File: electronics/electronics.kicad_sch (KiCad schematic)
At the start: 41 parts, among them J1 USB_C_Receptacle_USB2.0_14P, J2 AMT_102, J3 SPARK_MAX, J4 BLDC_FAN_ESC, SW1 RST, SW2 RST, SW3 SW_Push, SW4 SW_Push, SW5 SW_Push, SW6 SW_Push, U1 ESP32-S3-WROOM-1, U2 LSF0204, U3 AMS1117-3.3, U4 TPS62140, U5 AMS1117-3.3

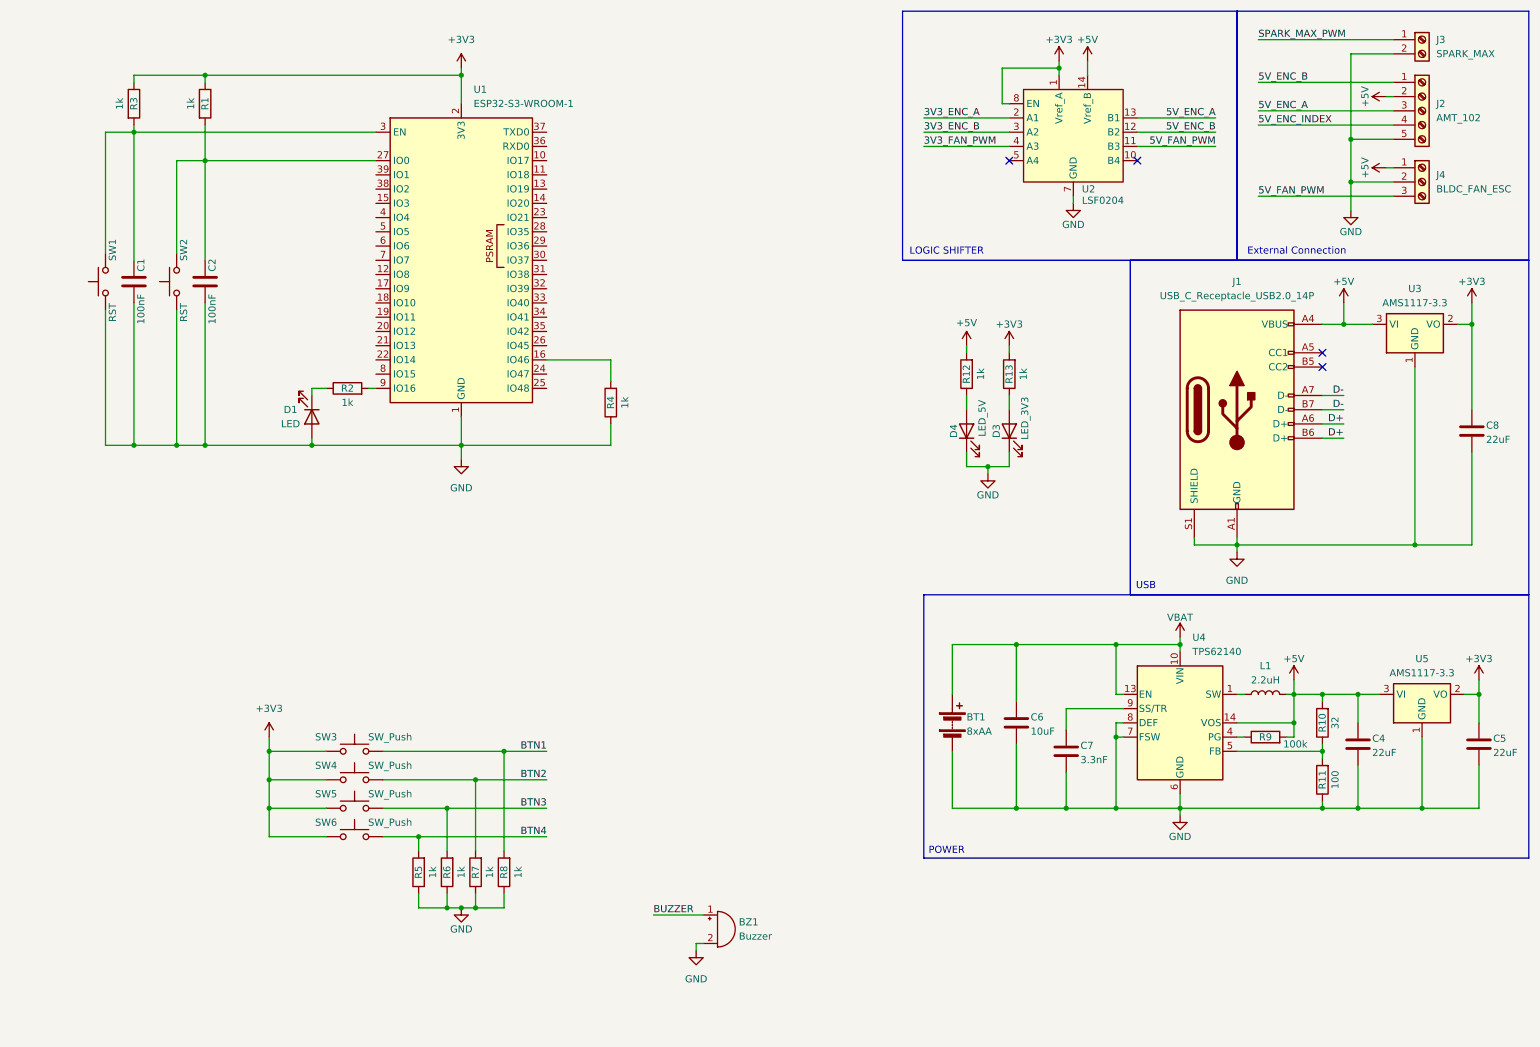
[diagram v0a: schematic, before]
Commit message: needs routing to decide pin placements
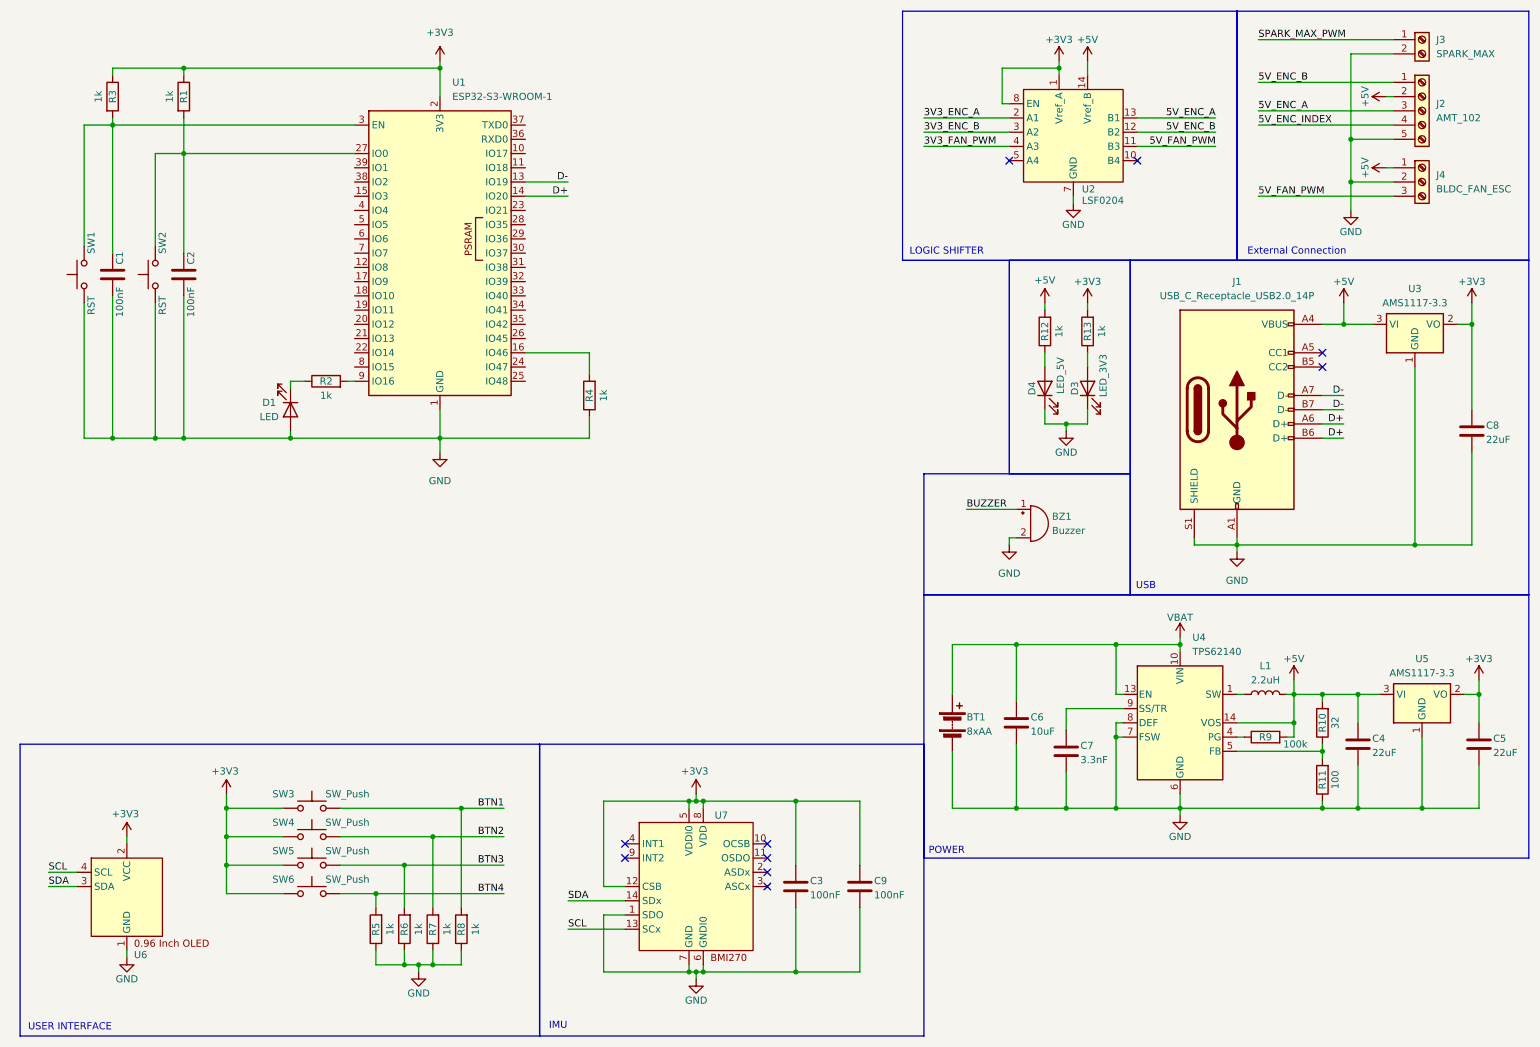
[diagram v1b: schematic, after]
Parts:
- added C3, C9: 100nF, symbol Device:C
- added U6: ~, Connector_PinHeader_2.54mm:PinHeader_1x04_P2.54mm_Vertical, symbol 0.96InchOLED:0.96_Inch_OLED
- added U7: ~, Package_LGA:Bosch_LGA-14_3x2.5mm_P0.5mm, symbol BMI270:BMI270
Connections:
- net +3V3: now also C3.1, C9.1, U6.2 (VCC), U7.12 (CSB), U7.5 (VDDI0), U7.8 (VDD)
- net D+: now also U1.14 (IO20)
- net D-: now also U1.13 (IO19)
- net GND: now also C3.2, C9.2, U6.1 (GND), U7.1 (SDO), U7.6 (GNDI0), U7.7 (GND)
- new net SCL: U6.4 (SCL), U7.13 (SCx)
- new net SDA: U6.3 (SDA), U7.14 (SDx)
- no-connect marks 4 -> 10
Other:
- note added: "IMU"
- note added: "USER INTERFACE"
- moved on the sheet: BZ1, C1, C2, D1, D3, D4, R1, R12, R13, R2, R3, R4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

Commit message: need to route switching psu correctly
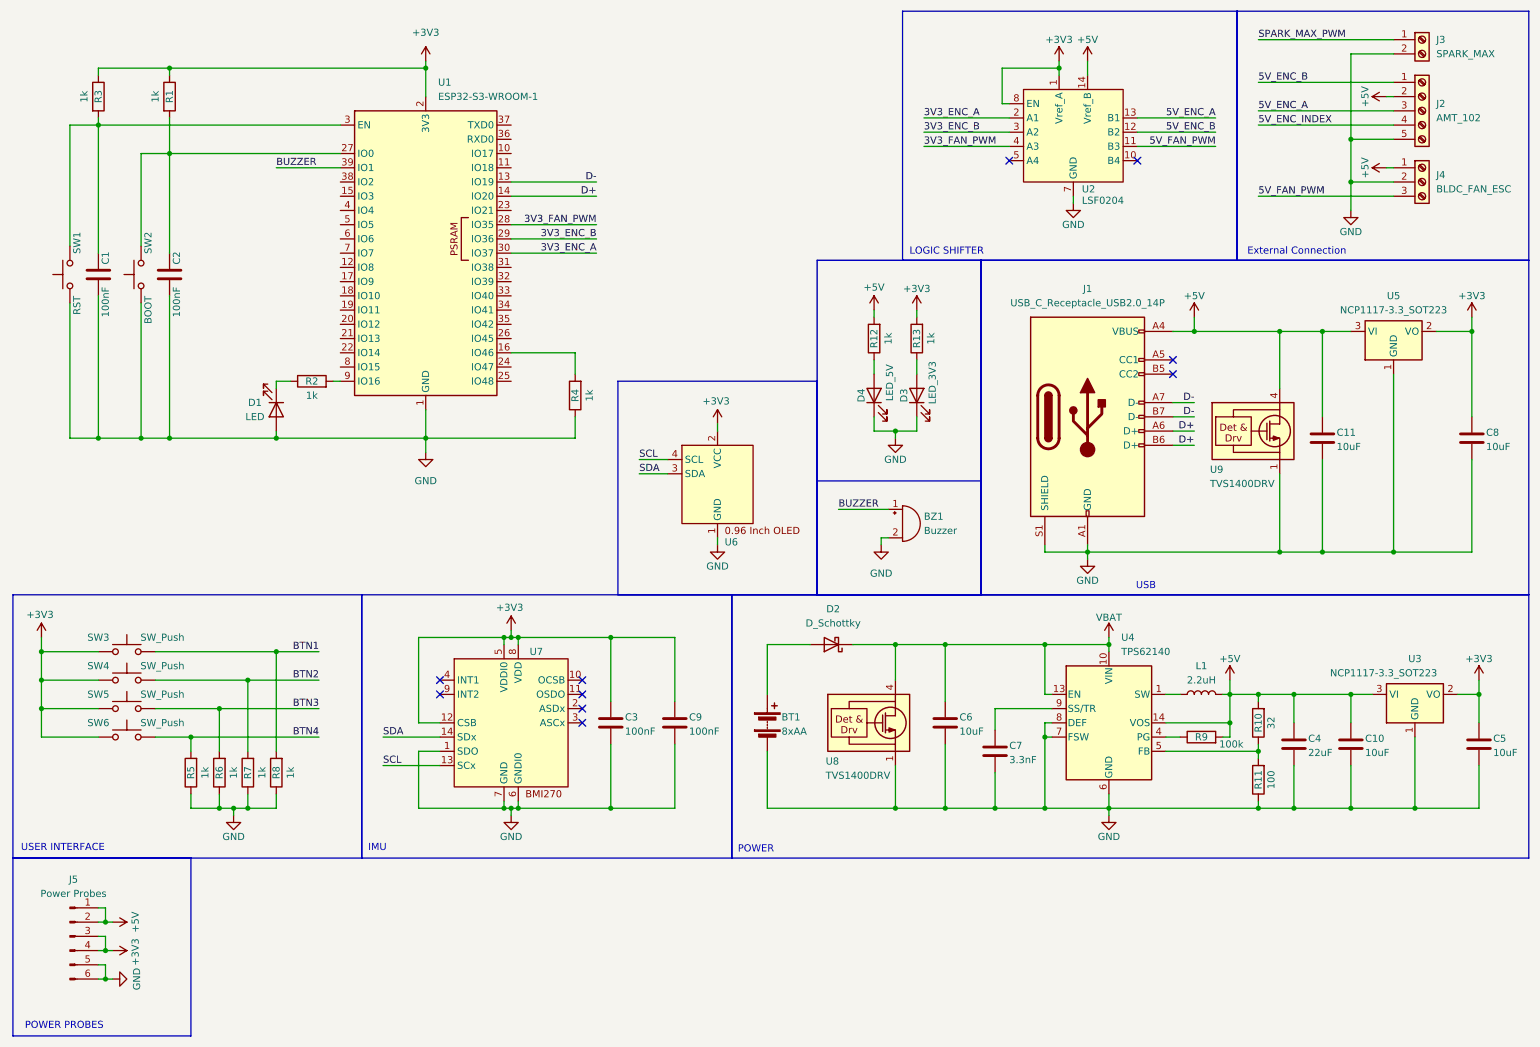
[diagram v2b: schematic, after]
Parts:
- removed U3, U5: AMS1117-3.3, Package_TO_SOT_SMD:SOT-223-3_TabPin2, symbol Regulator_Linear:AMS1117-3.3
- added C10, C11: 10uF, Capacitor_SMD:C_0603_1608Metric, symbol Device:C
- added D2: D_Schottky, Package_TO_SOT_SMD:TO-277A, symbol Device:D_Schottky
- added J5: Power Probes, Connector_PinSocket_2.54mm:PinSocket_1x06_P2.54mm_Vertical, symbol Connector:Conn_01x06_Pin
- added U3, U5: NCP1117-3.3_SOT223, Package_TO_SOT_SMD:SOT-223-3_TabPin2, symbol Regulator_Linear:NCP1117-3.3_SOT223
- added U8, U9: TVS1400DRV, Package_SON:WSON-6-1EP_2x2mm_P0.65mm_EP1x1.6mm_ThermalVias, symbol Power_Protection:TVS1400DRV
- BT1, J3: footprint (none) -> TerminalBlock_Phoenix:TerminalBlock_Phoenix_PT-1,5-2-5.0-H_1x02_P5.00mm_Horizontal
- BZ1: footprint (none) -> Buzzer_Beeper:Buzzer_12x9.5RM7.6
- C1, C2: footprint Capacitor_SMD:C_0201_0603Metric -> Capacitor_SMD:C_0603_1608Metric
- C3, C4, C6, C7, C9: footprint (none) -> Capacitor_SMD:C_0603_1608Metric
- C5, C8: value 22uF -> 10uF; footprint (none) -> Capacitor_SMD:C_0603_1608Metric
- J1: footprint (none) -> Connector_USB:USB_C_Receptacle_GCT_USB4110
- J2: footprint (none) -> TerminalBlock_Phoenix:TerminalBlock_Phoenix_PT-1,5-5-5.0-H_1x05_P5.00mm_Horizontal
- J4: footprint (none) -> TerminalBlock_Phoenix:TerminalBlock_Phoenix_PT-1,5-3-5.0-H_1x03_P5.00mm_Horizontal
- R1, R12, R13, R2, R3, R4, R5, R6, R7, R8: footprint Resistor_SMD:R_0201_0603Metric -> Resistor_SMD:R_0603_1608Metric
- R10, R11, R9: footprint (none) -> Resistor_SMD:R_0603_1608Metric
- SW1: footprint Button_Switch_SMD:SW_SPST_TL3342 -> Button_Switch_SMD:SW_SPST_EVQP2
- SW2: value RST -> BOOT; footprint Button_Switch_SMD:SW_SPST_TL3342 -> Button_Switch_SMD:SW_SPST_EVQP2
- SW3, SW4, SW5, SW6: footprint Button_Switch_Keyboard:SW_Cherry_MX_1.00u_PCB -> Button_Switch_SMD:SW_Push_1P1T_NO_6x6mm_H9.5mm
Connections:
- net +3V3: now also J5.3 (Pin_3), J5.4 (Pin_4), U3.2 (VO), U5.2 (VO)
- net +5V: now also C10.1, C11.1, J5.1 (Pin_1), J5.2 (Pin_2), U3.3 (VI), U5.3 (VI), U9.4 (IN), U9.5 (IN), U9.6 (IN)
- net 3V3_ENC_A: now also U1.30 (IO37)
- net 3V3_ENC_B: now also U1.29 (IO36)
- net 3V3_FAN_PWM: now also U1.28 (IO35)
- net BUZZER: now also U1.39 (IO1)
- net GND: now also C10.2, C11.2, J5.5 (Pin_5), J5.6 (Pin_6), U3.1 (GND), U5.1 (GND), U8.1 (GND), U8.2 (GND), U8.3 (GND), U8.7 (GND), U9.1 (GND), U9.2 (GND), U9.3 (GND), U9.7 (GND)
- net VBAT: now also D2.1 (K), U8.4 (IN), U8.5 (IN), U8.6 (IN); no longer BT1.1 (+)
- new net: BT1.1 (+), D2.2 (A)
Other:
- note added: "POWER PROBES"
- moved on the sheet: BT1, BZ1, C1, C2, C3, C4, C6, C7, C8, C9, D1, D3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

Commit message: ready to ship out
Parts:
- removed J5: Power Probes, Connector_PinSocket_2.54mm:PinSocket_1x06_P2.54mm_Vertical, symbol Connector:Conn_01x06_Pin
- added J5: Power Probes, Connector_PinHeader_2.54mm:PinHeader_1x04_P2.54mm_Vertical, symbol Connector:Conn_01x04_Pin
- C10, C11, C4, C5, C6, C8: footprint Capacitor_SMD:C_0603_1608Metric -> Capacitor_SMD:C_0805_2012Metric
- L1: footprint (none) -> Inductor_SMD:L_Vishay_IHLP-1212
- U7: value ~ -> BMI270
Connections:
- net +3V3: now also J5.2 (Pin_2)
- net +5V: now also J5.1 (Pin_1)
- net BTN1: now also U1.26 (IO45)
- net BTN2: now also U1.25 (IO48)
- net BTN3: now also U1.15 (IO3)
- net BTN4: now also U1.17 (IO9)
- net GND: now also J5.3 (Pin_3), J5.4 (Pin_4)
- net SCL: now also U1.18 (IO10)
- net SDA: now also U1.19 (IO11)
- net SPARK_MAX_PWM: now also U1.20 (IO12)
- net POWER_INDUCTOR: now reaches L1.1, U4.1 (SW), U4.2 (SW), U4.3 (SW)

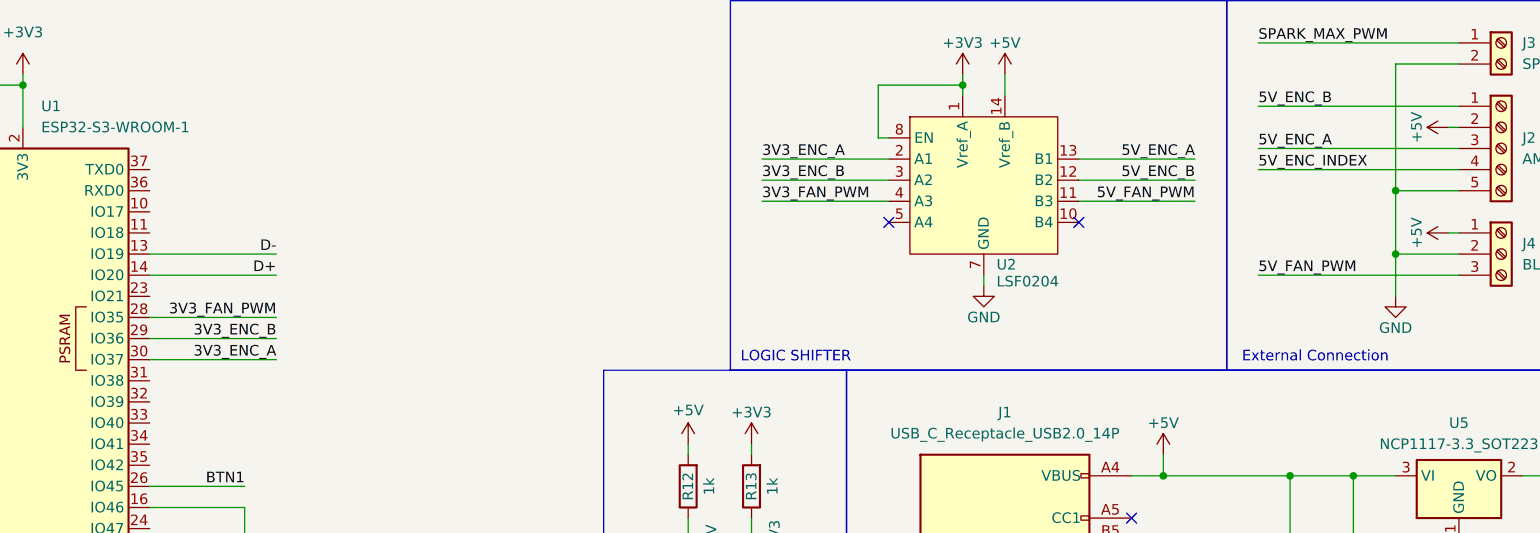
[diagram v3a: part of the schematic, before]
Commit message: added laser to pcb
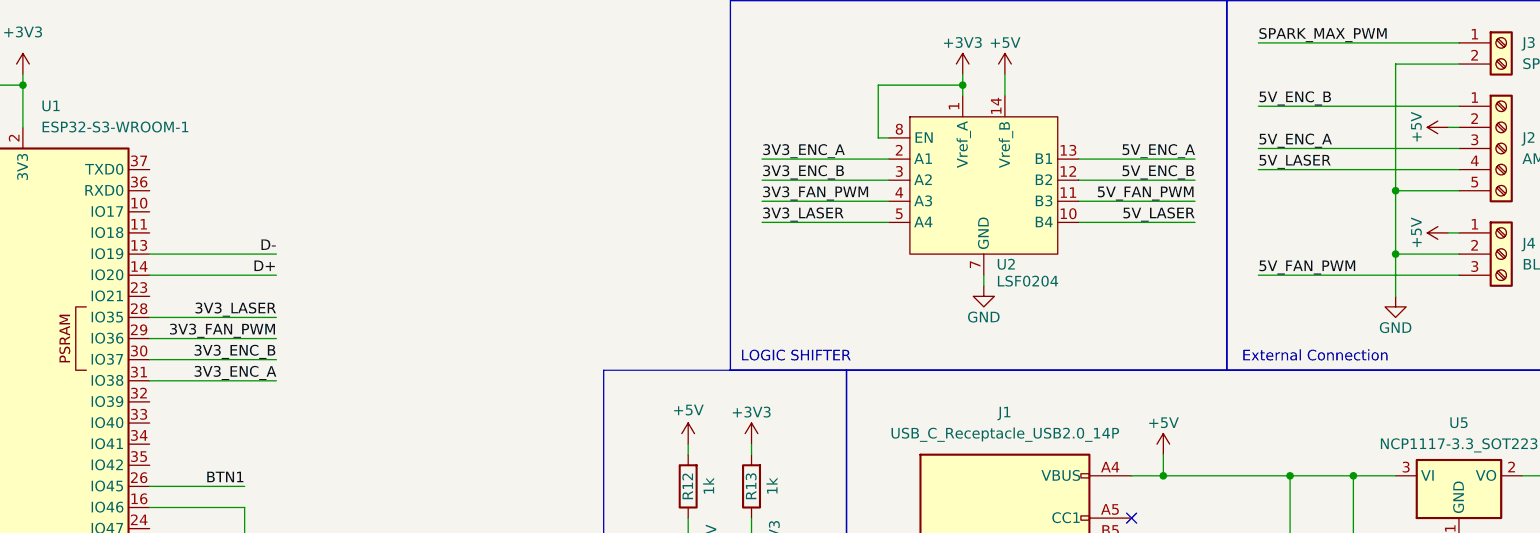
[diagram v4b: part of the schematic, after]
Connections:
- net 5V_ENC_INDEX is gone; now on net 5V_LASER: J2.4 (Pin_4)
- net 3V3_ENC_A: now also U1.31 (IO38); no longer U1.30 (IO37)
- net 3V3_ENC_B: now also U1.30 (IO37); no longer U1.29 (IO36)
- net 3V3_FAN_PWM: now also U1.29 (IO36); no longer U1.28 (IO35)
- net 5V_LASER: now reaches U2.10 (B4)
- net 3V3_LASER: now reaches U2.5 (A4)
- net 3V3_LASER: now also U1.28 (IO35)
- no-connect marks 10 -> 8

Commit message: transistor + ready
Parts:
- added Q1: MMBT100, Package_TO_SOT_SMD:SOT-23-3, symbol Simulation_SPICE:NPN
- added R14: 1k, Resistor_SMD:R_0603_1608Metric, symbol Device:R
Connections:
- net 5V_LASER: now also R14.1; no longer J2.4 (Pin_4)
- net GND: now also Q1.3 (E)
- new net: Q1.2 (B), R14.2
- new net LASER_GND: J2.4 (Pin_4), Q1.1 (C)
- no-connect marks 8 -> 27
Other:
- moved on the sheet: C1, C2, D1, R1, R2, R3, R4, SW1, SW2, U1, U2
